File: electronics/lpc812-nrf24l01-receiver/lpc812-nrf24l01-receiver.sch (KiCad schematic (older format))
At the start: 21 parts, among them K1 BAT, K2 CH3, K3 TH, K4 ST, P1 NRF24L01+, SW1 ISP/BIND, U1 MCP1703T-3302E/CB, U2 LPC812M101JDH16_TSSOP16, X1 12 MHz

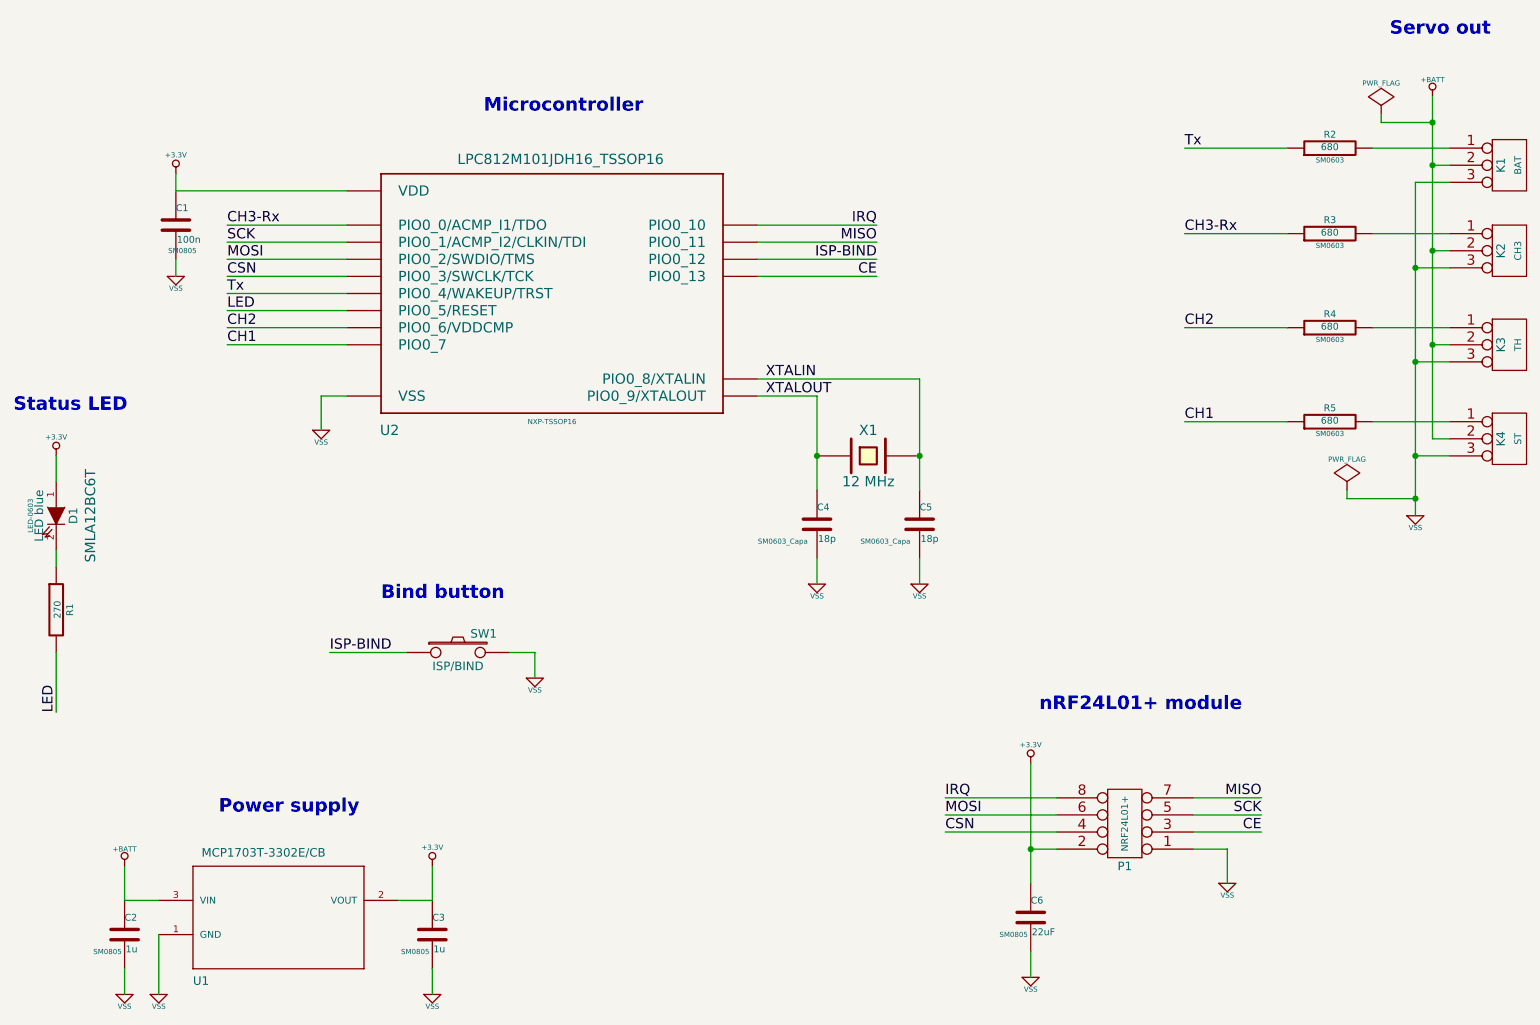
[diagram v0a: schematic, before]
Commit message: Start working on the silk screen
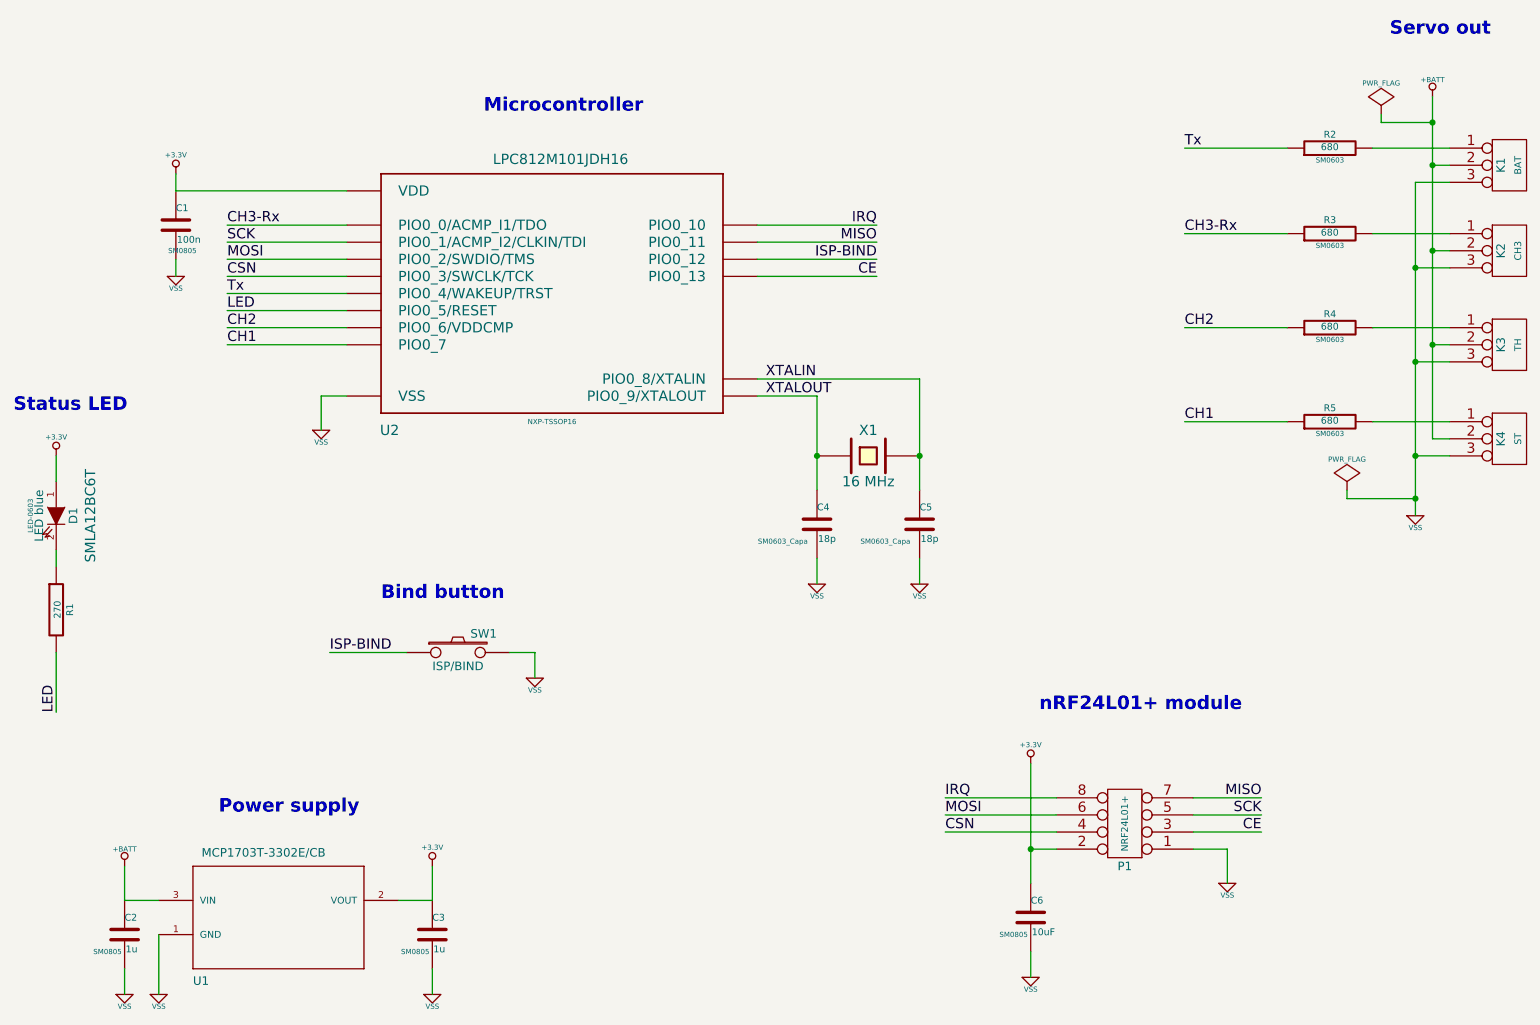
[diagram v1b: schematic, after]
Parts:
- C6: value 22uF -> 10uF
- U2: value LPC812M101JDH16_TSSOP16 -> LPC812M101JDH16
- X1: value 12 MHz -> 16 MHz
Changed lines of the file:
@@
 P 6450 3450
 F 0 "X1" H 6450 3600 60  0000 C CNN
-F 1 "12 MHz" H 6450 3300 60  0000 C CNN
+F 1 "16 MHz" H 6450 3300 60  0000 C CNN
 F 2 "crystal-SM49" H 6450 3450 60  0001 C CNN
 F 3 "~" H 6450 3450 60  0000 C CNN
@@
 P 4600 2450
 F 0 "U2" H 3650 1600 60  0000 C CNN
-F 1 "LPC812M101JDH16_TSSOP16" H 4650 3150 60  0000 C BNN
+F 1 "LPC812M101JDH16" H 4650 3150 60  0000 C BNN
 F 2 "NXP-TSSOP16" H 4600 1650 30  0000 C CNN
 F 3 "" H 4600 2450 60  0000 C CNN
@@
 P 7400 6150
 F 0 "C6" H 7400 6250 40  0000 L CNN
-F 1 "22uF" H 7406 6065 40  0000 L CNN
+F 1 "10uF" H 7406 6065 40  0000 L CNN
 F 2 "SM0805" H 7300 6050 30  0000 C CNN
 F 3 "~" H 7400 6150 60  0000 C CNN

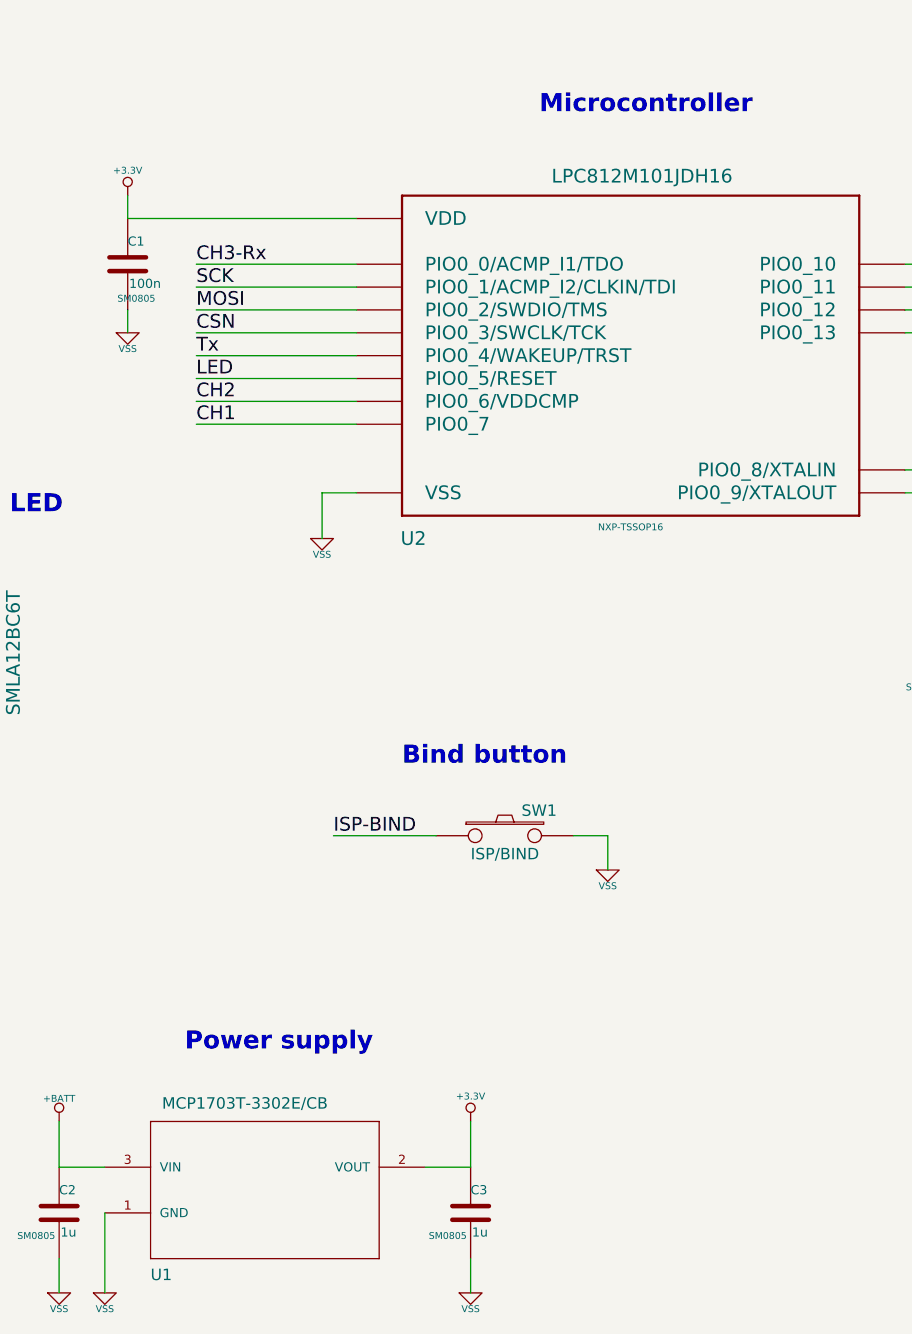
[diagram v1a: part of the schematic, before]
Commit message: More tweaking and playing around with silk screen and coordinates
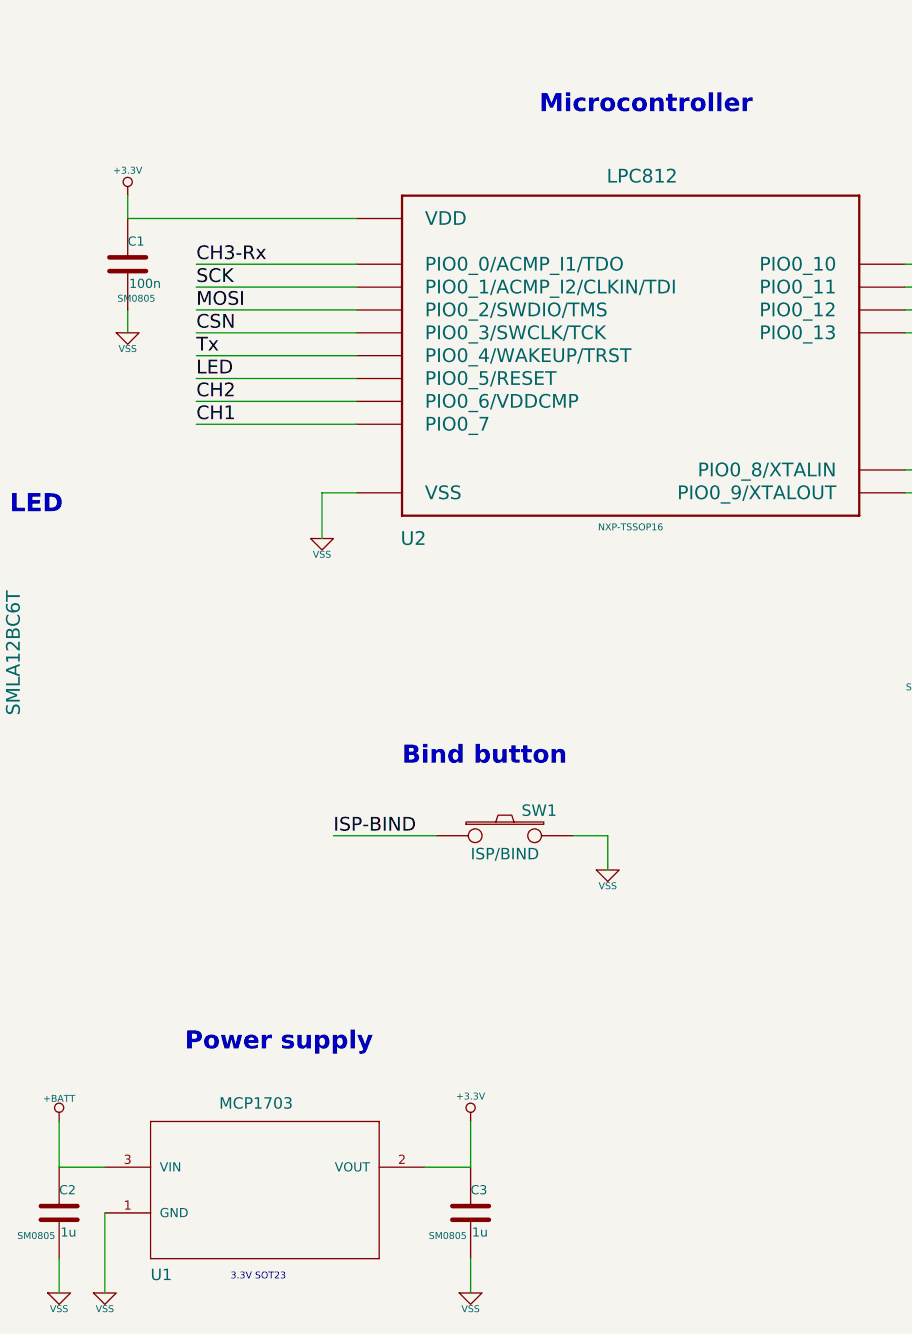
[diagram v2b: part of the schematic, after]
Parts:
- U1: value MCP1703T-3302E/CB -> MCP1703
- U2: value LPC812M101JDH16 -> LPC812
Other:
- note added: "3.3V SOT23"
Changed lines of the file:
@@
 Sheet 1 1
 Title ""
-Date "24 nov 2014"
+Date "25 nov 2014"
 Rev ""
 Comp ""
@@
 P 3000 6050
 F 0 "U1" H 2500 5550 50  0000 L BNN
-F 1 "MCP1703T-3302E/CB" H 2550 6300 50  0000 L BNN
+F 1 "MCP1703" H 2800 6300 50  0000 L BNN
 F 2 "MCP1703-SOT95P300X145-3N" H 3000 6200 50  0001 C CNN
 F 3 "" H 3000 6050 60  0000 C CNN
@@
 P 4600 2450
 F 0 "U2" H 3650 1600 60  0000 C CNN
-F 1 "LPC812M101JDH16" H 4650 3150 60  0000 C BNN
+F 1 "LPC812" H 4650 3150 60  0000 C BNN
 F 2 "NXP-TSSOP16" H 4600 1650 30  0000 C CNN
 F 3 "" H 4600 2450 60  0000 C CNN
@@
 Text Label 5850 3100 0    60   ~ 0
 XTALOUT
+Text Notes 2850 6550 0    30   ~ 0
+3.3V SOT23
 $EndSCHEMATC

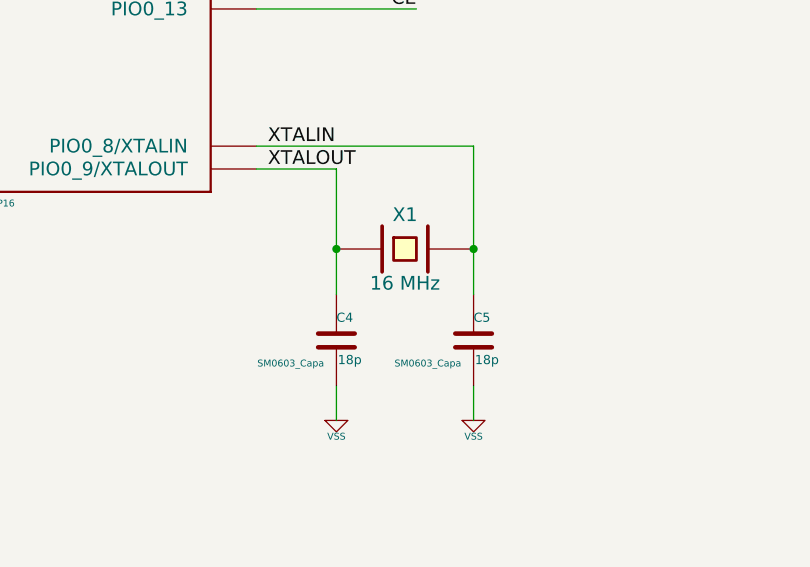
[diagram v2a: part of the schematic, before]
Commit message: Tweak board for least amount of vias; Add more silk screen
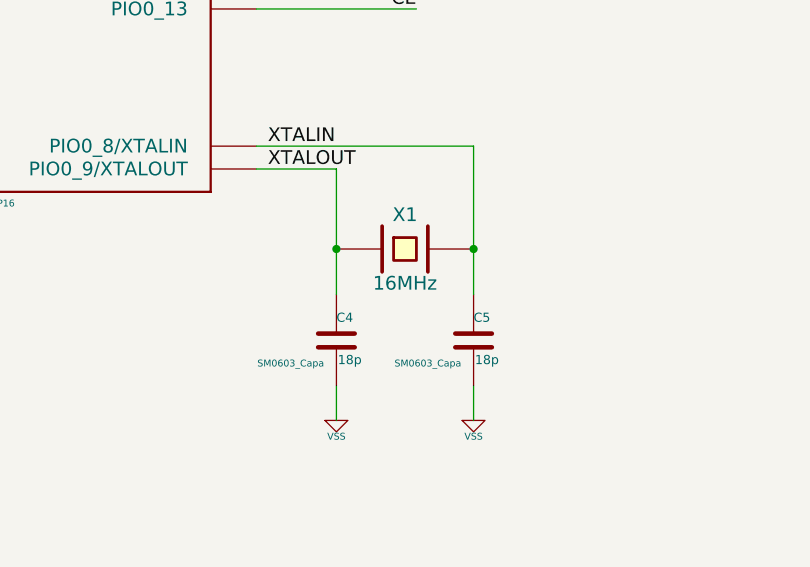
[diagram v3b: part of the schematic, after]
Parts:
- X1: value 16 MHz -> 16MHz
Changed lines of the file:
@@
 Sheet 1 1
 Title ""
-Date "25 nov 2014"
+Date "26 nov 2014"
 Rev ""
 Comp ""
@@
 P 6450 3450
 F 0 "X1" H 6450 3600 60  0000 C CNN
-F 1 "16 MHz" H 6450 3300 60  0000 C CNN
+F 1 "16MHz" H 6450 3300 60  0000 C CNN
 F 2 "crystal-SM49" H 6450 3450 60  0001 C CNN
 F 3 "~" H 6450 3450 60  0000 C CNN

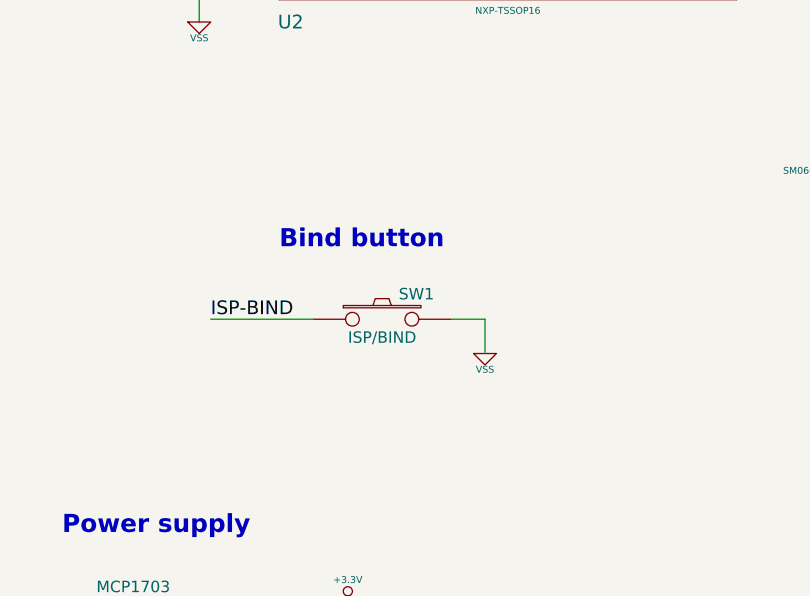
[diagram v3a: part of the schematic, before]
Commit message: Use Multicomp switches we have. Rename library to proper name
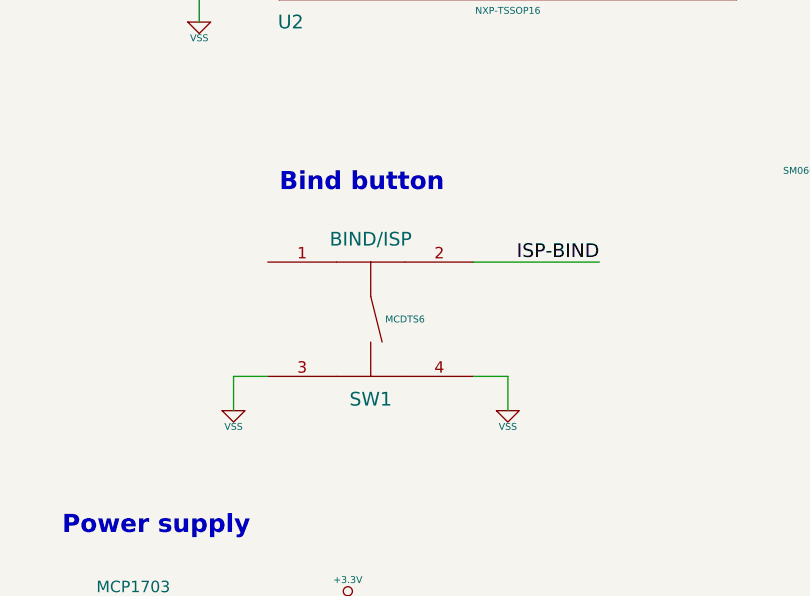
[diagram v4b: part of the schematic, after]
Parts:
- removed SW1: ISP/BIND, SW_PUSH_SMALL, symbol SW_PUSH
- added SW1: BIND/ISP, MCDTS6, symbol MCDTS6
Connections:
- net ISP-BIND: now also SW1.2
- net VSS: now also SW1.3, SW1.4
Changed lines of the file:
@@
 LIBS:LPC810
 LIBS:MCP1703
+LIBS:switches-multicomp
 LIBS:lpc812-nrf24l01-receiver-cache
 EELAYER 27 0
@@
 Sheet 1 1
 Title ""
-Date "26 nov 2014"
+Date "27 nov 2014"
 Rev ""
 Comp ""
@@
 $EndComp
 $Comp
-L SW_PUSH SW1
-U 1 1 546F0446
-P 4050 4600
-F 0 "SW1" H 4200 4710 50  0000 C CNN
-F 1 "ISP/BIND" H 4050 4520 50  0000 C CNN
-F 2 "SW_PUSH_SMALL" H 4050 4600 60  0001 C CNN
-F 3 "~" H 4050 4600 60  0000 C CNN
-	1    4050 4600
-	1    0    0    -1
-$EndComp
-$Comp
 L VSS #PWR015
 U 1 1 546F045D
-P 4500 4750
-F 0 "#PWR015" H 4500 4750 30  0001 C CNN
-F 1 "VSS" H 4500 4680 30  0000 C CNN
-F 2 "" H 4500 4750 60  0000 C CNN
-F 3 "" H 4500 4750 60  0000 C CNN
-	1    4500 4750
+P 4600 5000
+F 0 "#PWR015" H 4600 5000 30  0001 C CNN
+F 1 "VSS" H 4600 4930 30  0000 C CNN
+F 2 "" H 4600 5000 60  0000 C CNN
+F 3 "" H 4600 5000 60  0000 C CNN
+	1    4600 5000
 	1    0    0    -1
 $EndComp
@@
 	3400 2200 2700 2200
 Wire Wire Line
-	4350 4600 4500 4600
-Wire Wire Line
-	4500 4600 4500 4750
-Wire Wire Line
-	3750 4600 3300 4600
+	4450 4850 4600 4850
+Wire Wire Line
+	4600 4850 4600 5000
 Wire Wire Line
 	1700 3450 1700 3600
@@
 Text Notes 1450 3200 0    79   ~ 16
 Status LED
-Text Notes 3600 4300 0    79   ~ 16
+Text Notes 3600 4050 0    79   ~ 16
 Bind button
 Text Notes 2650 5550 0    79   ~ 16
@@
 Text Label 6500 2300 2    60   ~ 0
 ISP-BIND
-Text Label 3300 4600 0    60   ~ 0
+Text Label 5000 4350 2    60   ~ 0
 ISP-BIND
 Text Label 8300 1650 0    60   ~ 0
@@
 Text Notes 2850 6550 0    30   ~ 0
 3.3V SOT23
+$Comp
+L MCDTS6 SW1
+U 1 1 5476E67E
+P 4000 4600
+F 0 "SW1" H 4000 4250 60  0000 C CNN
+F 1 "BIND/ISP" H 4000 4950 60  0000 C CNN
+F 2 "MCDTS6" H 4150 4600 30  0000 C CNN
+F 3 "" H 4000 4600 60  0000 C CNN
+	1    4000 4600
+	1    0    0    -1
+$EndComp
+$Comp
+L VSS #PWR?
+U 1 1 5476E9E3
+P 3400 5000
+F 0 "#PWR?" H 3400 5000 30  0001 C CNN
+F 1 "VSS" H 3400 4930 30  0000 C CNN
+F 2 "" H 3400 5000 60  0000 C CNN
+F 3 "" H 3400 5000 60  0000 C CNN
+	1    3400 5000
+	1    0    0    -1
+$EndComp
+Wire Wire Line
+	3550 4850 3400 4850
+Wire Wire Line
+	3400 4850 3400 5000
+Wire Wire Line
+	4450 4350 5000 4350
 $EndSCHEMATC
